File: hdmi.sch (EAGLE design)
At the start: 136 parts, among them U0 6SLX45CSG324, U1 MT41J64M16, U2 TPD12S016RKTR, U3 TPD12S016RKTR, U4 TPD12S016RKTR, U5 MNR18, U6 MNR18

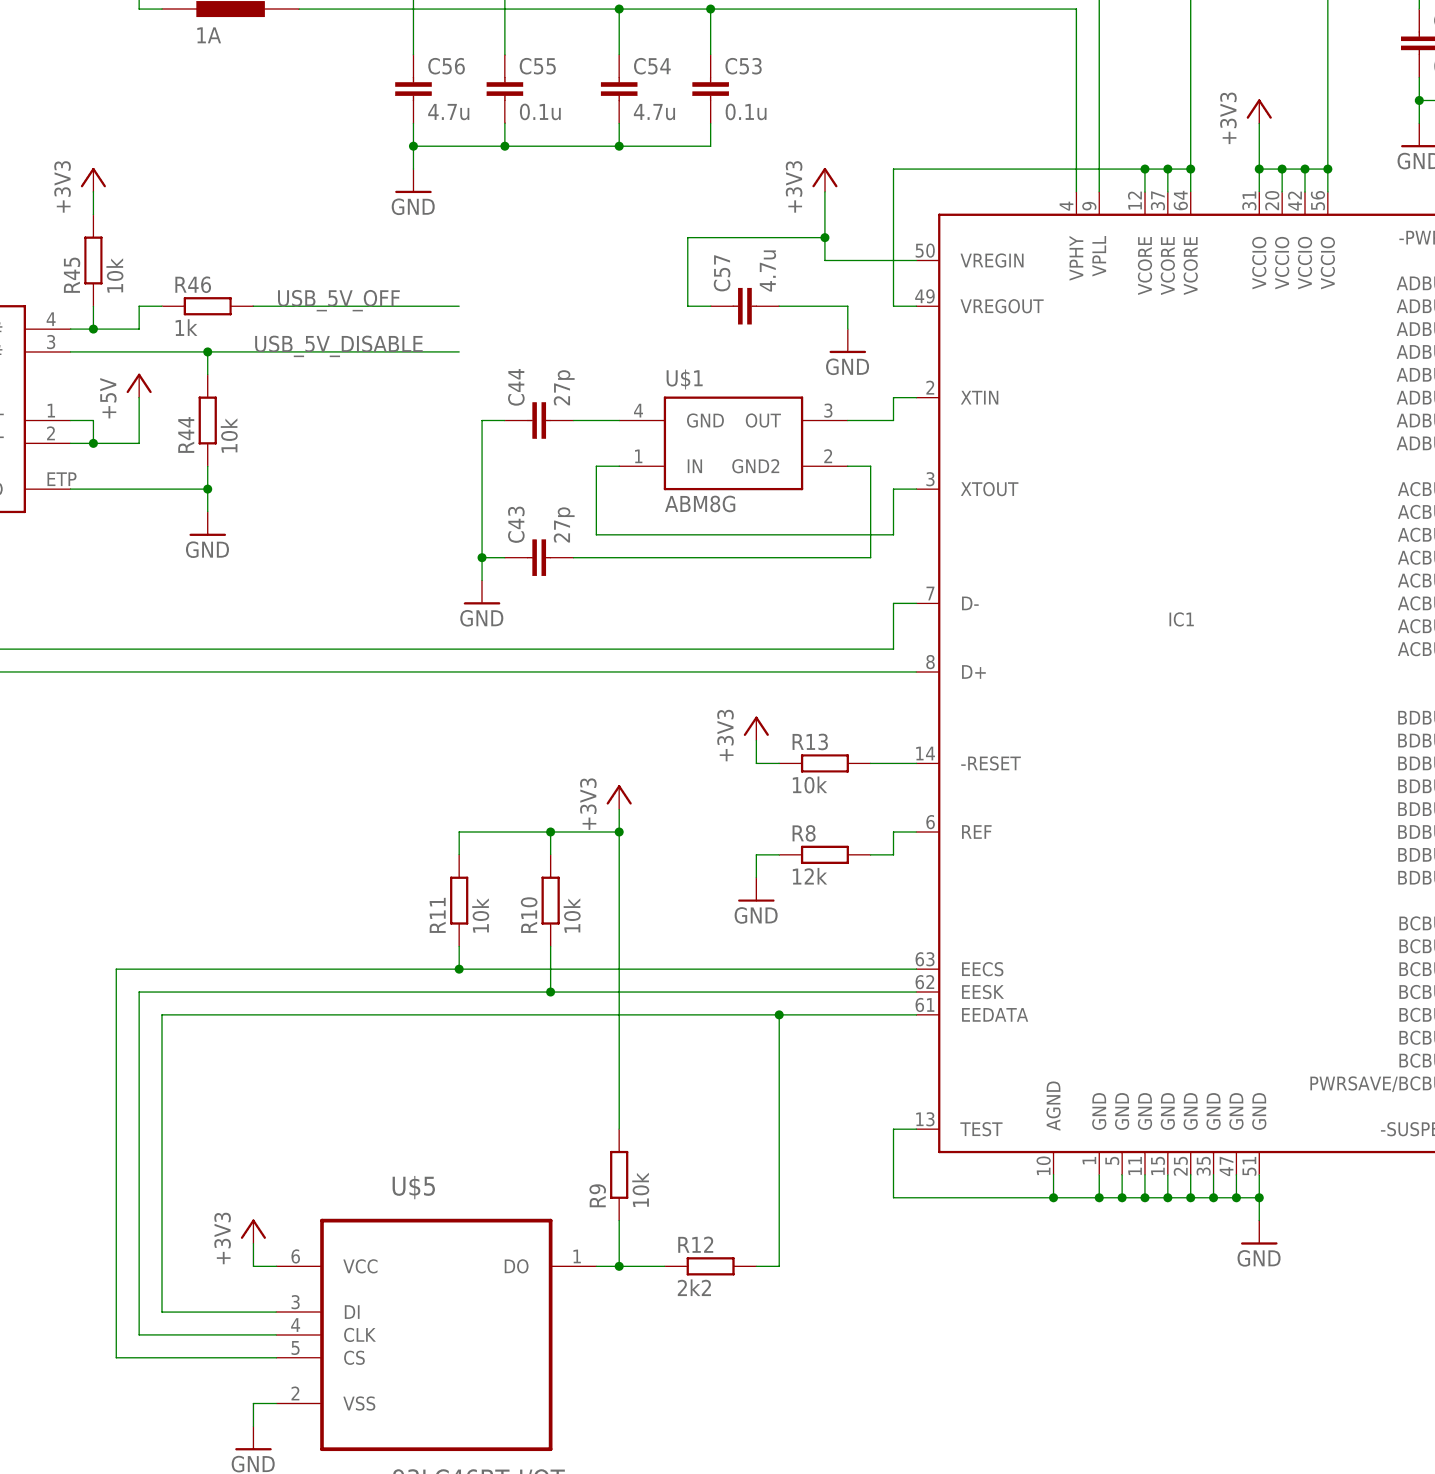
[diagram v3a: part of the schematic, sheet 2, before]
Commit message: +N-MOSFET at 5V supply, HDMI connector pin swap, minor wiring changes
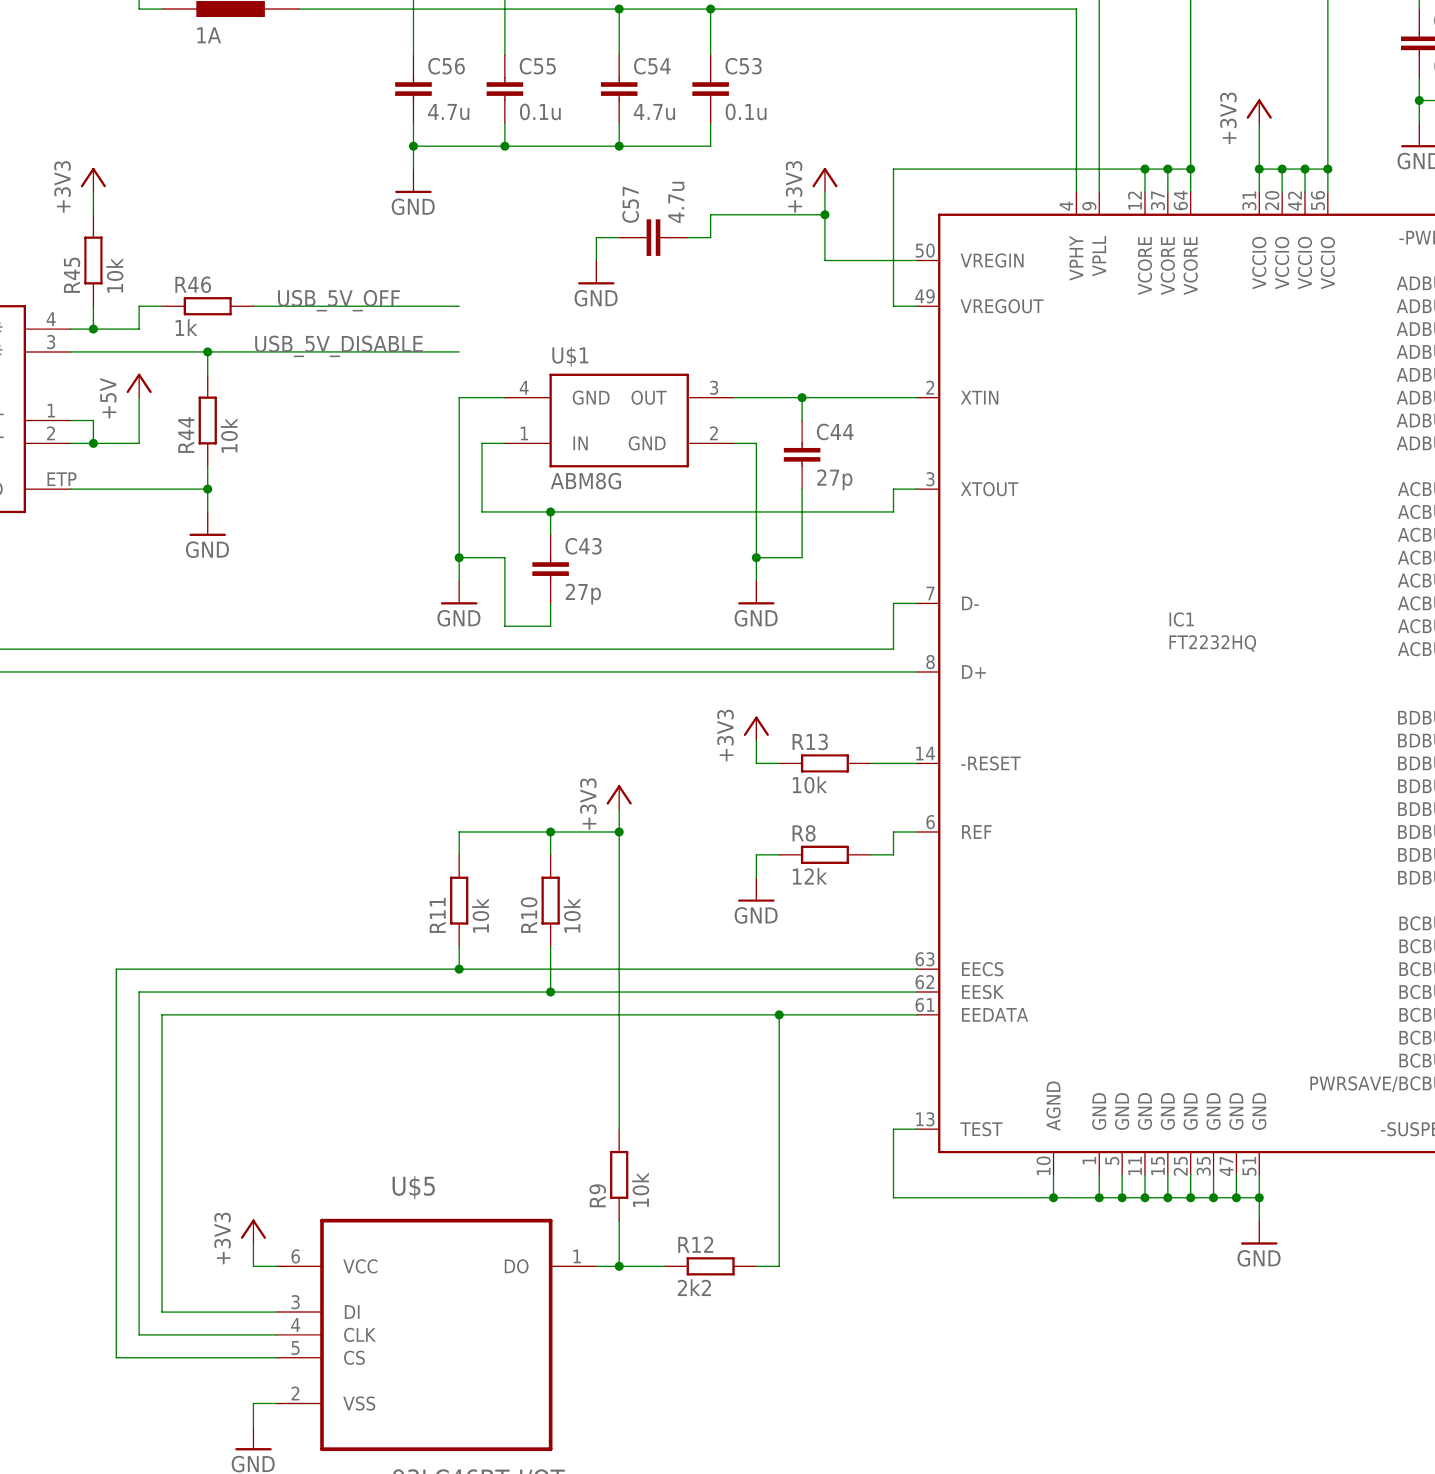
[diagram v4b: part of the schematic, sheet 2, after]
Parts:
- added Q1: N-MOSFETSOT23, prj-hdmi:N-MOSFETSOT23
- added R49: 1k, resistor:R-EU_R0402
- CONN3: value (none) -> USBMB-S
- IC1: value (none) -> FT2232HQ
- R47: value 50 -> 1k
- R48: value 100 -> 4.7k
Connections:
- removed net 3V3: C13.1, C14.1, C16.1, C17.1, C18.1, C20.1, C21.1, C22.1, C24.1, R29.2, U0B0.VCCO_0@0, U0B0.VCCO_0@1, U0B0.VCCO_0@2, U0B0.VCCO_0@3, U0B0.VCCO_0@4, U0B0.VCCO_0@5, U0B1.VCCO_1@0, U0B1.VCCO_1@1, U0B1.VCCO_1@2, U0B1.VCCO_1@3, U0B1.VCCO_1@4, U0B1.VCCO_1@5, U0B2.IO_L1N_M0_CMPMISO_2, U0B2.VCCO_2@0, U0B2.VCCO_2@1, U0B2.VCCO_2@2, U0B2.VCCO_2@3, U0B2.VCCO_2@4, U0B2.VCCO_2@5
- removed net 3V4: C25.1, C26.1, C27.1, C28.1, C33.1
- removed net 3V5: C29.1, C30.1, C31.1, C32.1
- removed net N$19: C52.2, R20.2
- removed net N$2: IC1.XTOUT, U$1.IN
- removed net N$4: C44.2, U$1.GND
- new net N$49: Q1.G, U$17.BFET
- new net OUT@8: Q1.S, R49.2, U$17.OUT@6, U$17.OUT@7, U$17.OUT@8
- net +1V2: now also C29.1, C30.1, C31.1, C32.1
- net +3V3: now also C13.1, C14.1, C16.1, C17.1, C18.1, C20.1, C21.1, C22.1, C24.1, C25.1, C26.1, C27.1, C28.1, C33.1, C57.2, R29.2, U0B0.VCCO_0@0, U0B0.VCCO_0@1, U0B0.VCCO_0@2, U0B0.VCCO_0@3, U0B0.VCCO_0@4, U0B0.VCCO_0@5, U0B1.VCCO_1@0, U0B1.VCCO_1@1, U0B1.VCCO_1@2, U0B1.VCCO_1@3, U0B1.VCCO_1@4, U0B1.VCCO_1@5, U0B2.IO_L1N_M0_CMPMISO_2, U0B2.VCCO_2@0, U0B2.VCCO_2@1, U0B2.VCCO_2@2, U0B2.VCCO_2@3, U0B2.VCCO_2@4, U0B2.VCCO_2@5; no longer C57.1
- net +5V: now also Q1.D; no longer U$17.OUT@6, U$17.OUT@7, U$17.OUT@8
- net DDR3_A12: now also U0B3.IO_L53N_M3A12_3
- net DDR3_DQ3: now also U1.DQ3
- net DDR3_DQ4: no longer U1.DQ3
- net GND: now also C43.2, C44.2, C52.2, C57.1, R20.2, U$1.GND@2, U$1.GND@4; no longer C43.1, C44.1, C57.2
- net HDMI_RX0_CEC: now also U2.CEC_B; no longer U2.CEC_A
- net HDMI_RX0_CEC_3V3: now also U2.CEC_A; no longer U2.CEC_B
- net HDMI_RX0_SCL_3V3: now also U2.SCL_A; no longer U2.SCL_B
- net HDMI_RX0_SCL_5V: now also U2.SCL_B; no longer U2.SCL_A
- net HDMI_RX0_SDA_3V3: now also U2.SDA_A; no longer U2.SDA_B
- net HDMI_RX0_SDA_5V: now also U2.SDA_B; no longer U2.SDA_A
- net HDMI_RX1_CEC: now also U3.CEC_B; no longer U3.CEC_A
- net HDMI_RX1_CEC_3V3: now also U3.CEC_A; no longer U3.CEC_B
- net HDMI_RX1_SCL_3V3: now also U3.SCL_A; no longer U3.SCL_B
- net HDMI_RX1_SCL_5V: now also U3.SCL_B; no longer U3.SCL_A
- net HDMI_RX1_SDA_3V3: now also U3.SDA_A; no longer U3.SDA_B
- net HDMI_RX1_SDA_5V: now also U3.SDA_B; no longer U3.SDA_A
- net HDMI_TX0_CEC: now also U4.CEC_B; no longer U4.CEC_A
- net HDMI_TX0_CEC_3V3: now also U4.CEC_A; no longer U4.CEC_B
- net HDMI_TX0_HPD_3V3: now also U4.HPD_A; no longer U4.HPD_B
- net HDMI_TX0_HPD_5V: now also U4.HPD_B; no longer U4.HPD_A
- net HDMI_TX0_SCL_3V3: now also U4.SCL_A; no longer U4.SCL_B
- net HDMI_TX0_SCL_5V: now also U4.SCL_B; no longer U4.SCL_A
- net HDMI_TX0_SDA_3V3: now also U4.SDA_A; no longer U4.SDA_B
- net HDMI_TX0_SDA_5V: now also U4.SDA_B; no longer U4.SDA_A
- net N$1: now also C44.1
- net N$10: now also U$5.DI
- net N$5: now also C43.1, IC1.XTOUT, U$1.IN; no longer C43.2, U$1.GND2
- net USB_5V_DISABLE: now also R49.1
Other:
- moved on the sheet: C43, C44, C57, R41, U$1

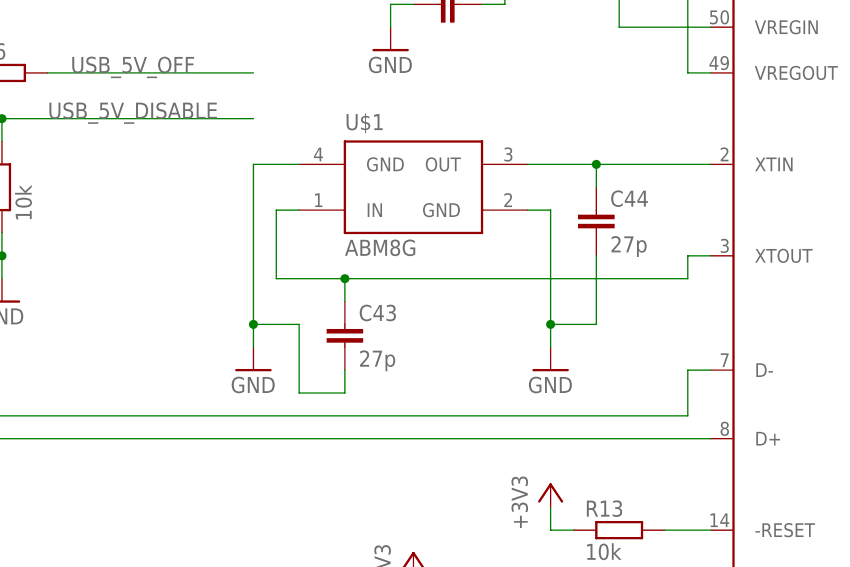
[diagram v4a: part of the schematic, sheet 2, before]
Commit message: +Oscillator
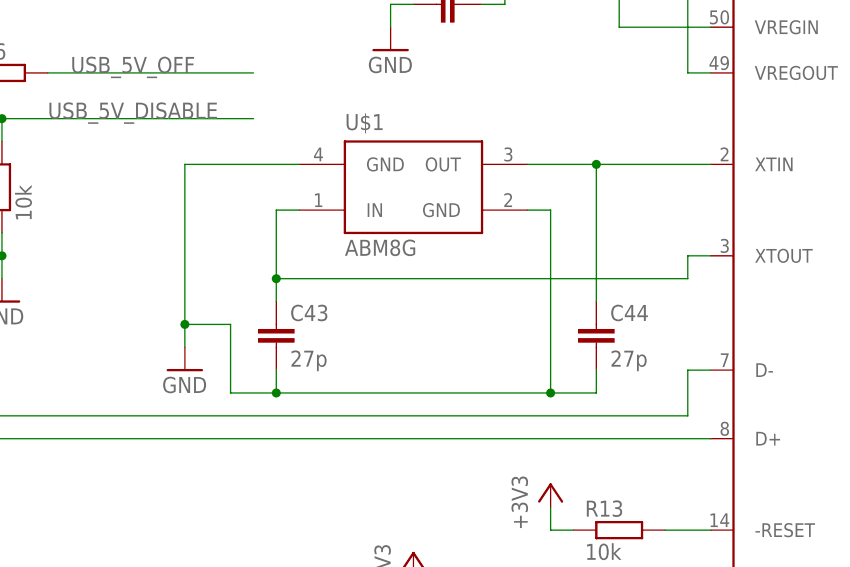
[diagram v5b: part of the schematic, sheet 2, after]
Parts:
- added C23: 0.1u, rcl:C-EUC0402
- added U7: 20Mhz, prj-hdmi:OSCILLATOR2.5X2
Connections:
- new net FPGA_OSC: U0B2.IO_L29N_GCLK2_2, U7.OUT
- net +3V3: now also C23.1, U7.EN, U7.VCC
- net GND: now also C23.2, U7.GND
- net HDMI_TX0_CEC_3V3: now also U0B2.IO_L40N_2; no longer U0B2.IO_L29N_GCLK2_2
- net HDMI_TX0_HPD_3V3: now also U0B2.IO_L40P_2; no longer U0B2.IO_L29P_GCLK3_2
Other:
- moved on the sheet: C43, C44

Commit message: +IO
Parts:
- removed C23: 0.1u, rcl:C-EUC0402
- removed U7: 20Mhz, prj-hdmi:OSCILLATOR2.5X2
- added C49: 0.1u, rcl:C-EUC0402
- added SV1: JTAG, prj-hdmi:MA06-1
- added SV2: FE10-2, prj-hdmi:FE10-2
- added U$12: SN74LVC8T245RHLR, prj-hdmi:SN74LVC8T245RHLR
- added U8: 20Mhz, prj-hdmi:OSCILLATOR2.5X2
- L1, L2, L3: value 1u, 2.3A -> 1u, 3A
- R44: value 10k -> 4.7k
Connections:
- removed net FPGA_OSC: U0B2.IO_L29N_GCLK2_2, U7.OUT
- removed net USB_PWREN#: IC1.-PWREN
- new net FPGA_OSC1: U0B0.IO_L35N_GCLK16_0, U8.OUT
- new net IO_0: SV2.5, U0B0.IO_L39P_0
- new net IO_1: SV2.7, U0B0.IO_L39N_0
- new net IO_10: U$12.A3, U0B0.IO_L64P_SCP5_0
- new net IO_10_5V: SV2.10, U$12.B3
- new net IO_11: U$12.A4, U0B0.IO_L64N_SCP4_0
- new net IO_11_5V: SV2.12, U$12.B4
- new net IO_12: U$12.A5, U0B0.IO_L65P_SCP3_0
- new net IO_12_5V: SV2.14, U$12.B5
- new net IO_13: U$12.A6, U0B0.IO_L65N_SCP2_0
- new net IO_13_5V: SV2.16, U$12.B6
- new net IO_14: U$12.A7, U0B0.IO_L66P_SCP1_0
- new net IO_14_5V: SV2.18, U$12.B7
- new net IO_15: U$12.A8, U0B0.IO_L66N_SCP0_0
- new net IO_15_5V: SV2.20, U$12.B8
- new net IO_2: SV2.9, U0B0.IO_L41P_0
- new net IO_3: SV2.11, U0B0.IO_L41N_0
- new net IO_4: SV2.13, U0B0.IO_L50P_0
- new net IO_5: SV2.15, U0B0.IO_L50N_0
- new net IO_6: SV2.17, U0B0.IO_L62P_0
- new net IO_7: SV2.19, U0B0.IO_L62N_VREF_0
- new net IO_8: U$12.A1, U0B0.IO_L63P_SCP7_0
- new net IO_8-15_DIR: U$12.DIR, U0B0.IO_L38N_VREF_0
- new net IO_8-15_DISABLE: U$12.OE#, U0B0.IO_L38P_0
- new net IO_8_5V: SV2.6, U$12.B1
- new net IO_9: U$12.A2, U0B0.IO_L63N_SCP6_0
- new net IO_9_5V: SV2.8, U$12.B2
- net +3V3: now also C49.1, SV1.1, SV2.1, U$12.VCCA, U8.EN, U8.VCC; no longer C23.1, U7.EN, U7.VCC
- net +5V: now also SV2.2, U$12.VCCB@1, U$12.VCCB@2
- net GND: now also C49.2, SV1.2, SV2.3, SV2.4, U$12.ETP, U$12.GND@1, U$12.GND@2, U$12.GND@3, U8.GND; no longer C23.2, U7.GND
- net USB_5V_OFF: now also U0B1.IO_L36P_A9_M1BA0_1
- net USB_SUSPEND#: now also U0B1.IO_L36N_A8_M1BA1_1
- net USB_TCK: now also SV1.3
- net USB_TDI: now also SV1.5
- net USB_TDO: now also SV1.4
- net USB_TMS: now also SV1.6

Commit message: switched from hot swap controller to buck regulator, +PMOD
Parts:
- removed Q1: N-MOSFETSOT23, prj-hdmi:N-MOSFETSOT23
- removed R42: 47k, resistor:R-EU_R0402
- removed R47, R49: 1k, resistor:R-EU_R0402
- removed SV2: FE10-2, prj-hdmi:FE10-2
- removed U$17: TPS2592BA, prj-hdmi:TPS2592BA
- added JP1: 5V_SEL, prj-hdmi:JP2W
- added JP2: PMOD0-1_VCC_SEL, prj-hdmi:JP2E
- added JP3: PMOD2-3_VCC_SEL, prj-hdmi:JP2E
- added L7: 3.3u, 4A, prj-hdmi:INDUCTOR1008
- added SV3: EXT_SUP, prj-hdmi:MA02-1
- added U$13: PMOD-2X6, prj-hdmi:PMOD-2X6
- C15: value 0.47n -> 0.1u; device rcl:C-EUC0402 -> prj-hdmi:C-EU0603
- C19: value 0.1u -> 10u
- C7: value 100u -> 10u; device prj-hdmi:C-EU0603 -> prj-hdmi:C-EU0402
- R44: value 4.7k -> 10k
- R48: value 4.7k -> 10k; device resistor:R-EU_R0402 -> prj-hdmi:R-EU_0402
- U$11: value 20V -> MIC24085; device prj-hdmi:ZENER-DIODESOD123FL -> prj-hdmi:MIC24085
- U$12: value SN74LVC8T245RHLR -> PMOD-2X6; device prj-hdmi:SN74LVC8T245RHLR -> prj-hdmi:PMOD-2X6
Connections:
- removed net IO_0: SV2.5, U0B0.IO_L39P_0
- removed net IO_1: SV2.7, U0B0.IO_L39N_0
- removed net IO_10: U$12.A3, U0B0.IO_L64P_SCP5_0
- removed net IO_10_5V: SV2.10, U$12.B3
- removed net IO_11: U$12.A4, U0B0.IO_L64N_SCP4_0
- removed net IO_11_5V: SV2.12, U$12.B4
- removed net IO_12: U$12.A5, U0B0.IO_L65P_SCP3_0
- removed net IO_12_5V: SV2.14, U$12.B5
- removed net IO_13: U$12.A6, U0B0.IO_L65N_SCP2_0
- removed net IO_13_5V: SV2.16, U$12.B6
- removed net IO_14: U$12.A7, U0B0.IO_L66P_SCP1_0
- removed net IO_14_5V: SV2.18, U$12.B7
- removed net IO_15: U$12.A8, U0B0.IO_L66N_SCP0_0
- removed net IO_15_5V: SV2.20, U$12.B8
- removed net IO_2: SV2.9, U0B0.IO_L41P_0
- removed net IO_3: SV2.11, U0B0.IO_L41N_0
- removed net IO_4: SV2.13, U0B0.IO_L50P_0
- removed net IO_5: SV2.15, U0B0.IO_L50N_0
- removed net IO_6: SV2.17, U0B0.IO_L62P_0
- removed net IO_7: SV2.19, U0B0.IO_L62N_VREF_0
- removed net IO_8: U$12.A1, U0B0.IO_L63P_SCP7_0
- removed net IO_8-15_DIR: U$12.DIR, U0B0.IO_L38N_VREF_0
- removed net IO_8-15_DISABLE: U$12.OE#, U0B0.IO_L38P_0
- removed net IO_8_5V: SV2.6, U$12.B1
- removed net IO_9: U$12.A2, U0B0.IO_L63N_SCP6_0
- removed net IO_9_5V: SV2.8, U$12.B2
- removed net N$32: C15.1, U$17.DV/DT
- removed net N$36: R42.2, U$17.ILIM
- removed net OUT@8: Q1.S, R49.2, U$17.OUT@6, U$17.OUT@7, U$17.OUT@8
- new net N$2: C15.1, U$11.BST
- new net N$51: JP2.2, U$12.12, U$12.6
- new net PMOD0_0: U$12.1, U0B0.IO_L39P_0
- new net PMOD0_1: U$12.2, U0B0.IO_L39N_0
- new net PMOD0_2: U$12.3, U0B0.IO_L41P_0
- new net PMOD0_3: U$12.4, U0B0.IO_L41N_0
- new net PMOD1_0: U$12.7, U0B0.IO_L50P_0
- new net PMOD1_1: U$12.8, U0B0.IO_L50N_0
- new net PMOD1_2: U$12.9, U0B0.IO_L62P_0
- new net PMOD1_3: U$12.10, U0B0.IO_L62N_VREF_0
- new net PMOD2_0: U$13.1, U0B0.IO_L63P_SCP7_0
- new net PMOD2_1: U$13.2, U0B0.IO_L63N_SCP6_0
- new net PMOD2_2: U$13.3, U0B0.IO_L64P_SCP5_0
- new net PMOD2_3: U$13.4, U0B0.IO_L64N_SCP4_0
- new net PMOD3_0: U$13.7, U0B0.IO_L65P_SCP3_0
- new net PMOD3_1: U$13.8, U0B0.IO_L65N_SCP2_0
- new net PMOD3_2: U$13.9, U0B0.IO_L66P_SCP1_0
- new net PMOD3_3: U$13.10, U0B0.IO_L66N_SCP0_0
- new net SW@16: C15.2, L7.1, U$11.SW@1, U$11.SW@12, U$11.SW@13, U$11.SW@16
- new net USB_VBUS: JP1.3, U$10.VBUS_OUT@1, U$10.VBUS_OUT@2
- net +3V3: now also JP2.1, JP3.1; no longer SV2.1, U$12.VCCA
- net +5V: now also JP1.2, JP2.3, JP3.3; no longer Q1.D, SV2.2, U$10.VBUS_OUT@1, U$10.VBUS_OUT@2, U$12.VCCB@1, U$12.VCCB@2
- net CENTER: now also SV3.1; no longer U$11.C
- net GND: now also SV3.2, U$11.ETP, U$11.GND, U$11.PGND@14, U$11.PGND@15, U$12.11, U$12.5, U$13.11, U$13.5; no longer C15.2, R42.1, R48.1, SV2.3, SV2.4, U$11.A, U$12.ETP, U$12.GND@1, U$12.GND@2, U$12.GND@3, U$17.GND
- net N$29: now also R48.2, U$11.VCC@11, U$11.VCC@2, U$11.VCC@3; no longer R47.2, U$17.VIN@3, U$17.VIN@4, U$17.VIN@5
- net N$30: now also JP1.1, L7.2, U$11.FB; no longer R47.1, R48.2, U$17.EN/EVLO
- net N$49: now also JP3.2, U$13.12, U$13.6; no longer Q1.G, U$17.BFET
- net USB_5V_DISABLE: now also R48.1, U$11.PG; no longer R49.1
